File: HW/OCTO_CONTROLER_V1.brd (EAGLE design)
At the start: 65 x 56 mm, 58 parts, among them IC1 CXDM4060P, IC2 AOZ1284PI, J1 DC_POWER, Q1 CXDM4060P, Q10 DTDG23YP, Q2 CXDM4060P, Q3 DTC114EUA, Q4 DTC114EUA, Q5 DTC114EUA, Q6 DTC114EUA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

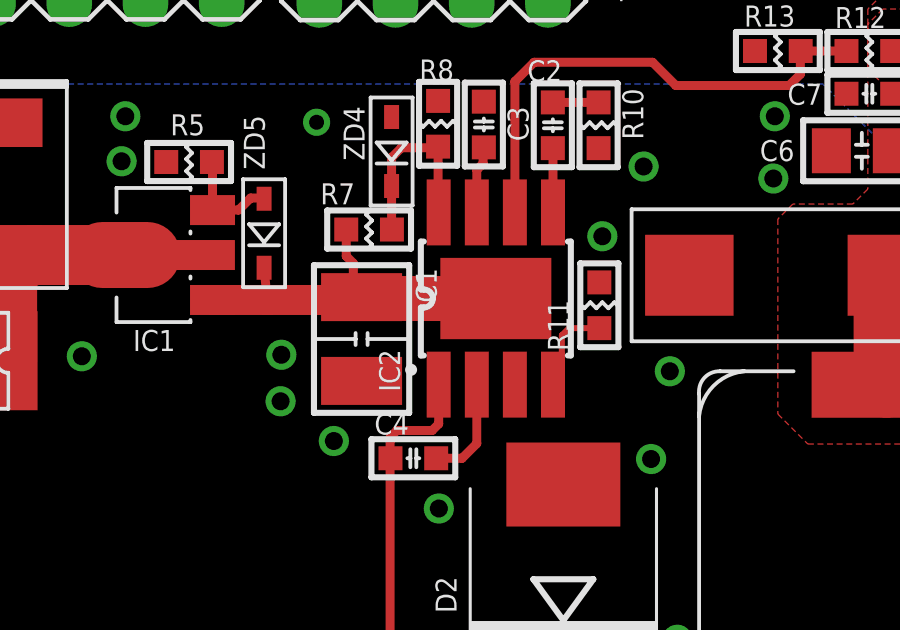
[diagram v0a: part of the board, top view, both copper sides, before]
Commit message: LED 저항값 수정
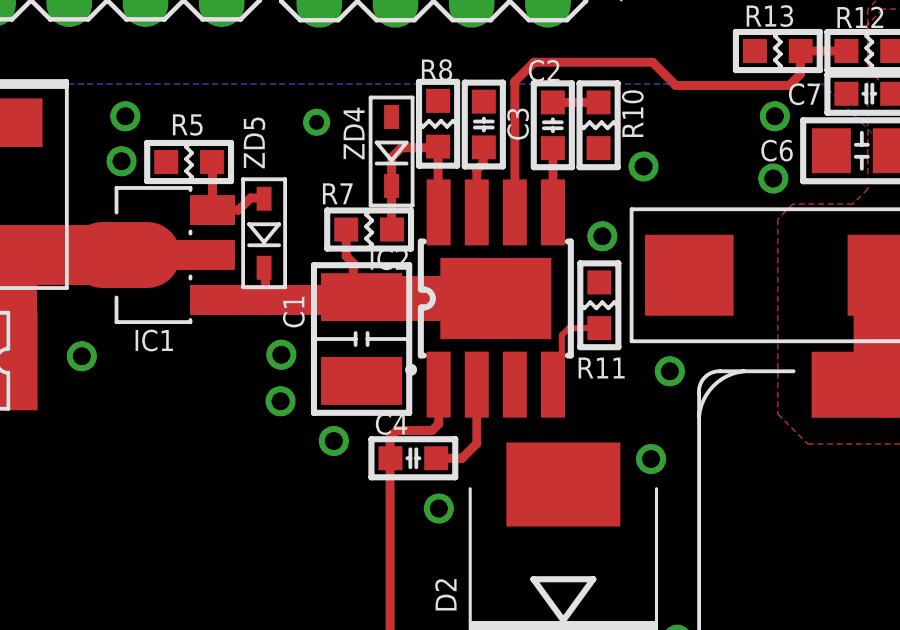
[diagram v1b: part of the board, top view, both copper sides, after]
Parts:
- R11: value 46.6k -> 47k
- R3, R4, R6, R9: value 220 -> 300
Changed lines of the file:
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@@
 </element>
 <element name="IC2" library="cona_lib" package="S08-EP1" value="AOZ1284PI" x="-14.9" y="23.35" smashed="yes">
-<attribute name="NAME" x="-18.092" y="20.245" size="0.7" layer="25" rot="R90"/>
+<attribute name="NAME" x="-17.745" y="25.008" size="0.7" layer="25" rot="R180"/>
 <attribute name="VALUE" x="-11.263" y="21.445" size="0.7" layer="27" rot="R90"/>
 </element>
@@
 <attribute name="VALUE" x="-11.476" y="27.601" size="0.7" layer="27" rot="R90"/>
 </element>
-<element name="R11" library="cona_lib" package="R0603" value="46.6k" x="-11.45" y="23.125" smashed="yes" rot="R90">
-<attribute name="NAME" x="-12.466" y="21.601" size="0.7" layer="25" rot="R90"/>
+<element name="R11" library="cona_lib" package="R0603" value="47k" x="-11.45" y="23.125" smashed="yes" rot="R90">
+<attribute name="NAME" x="-10.526" y="21.384" size="0.7" layer="25" rot="R180"/>
 <attribute name="VALUE" x="-9.926" y="21.601" size="0.7" layer="27" ratio="10" rot="R90"/>
 </element>
@@
 </element>
 <element name="C1" library="cona_lib" package="C3225" value="10uF/35V" x="-19.375" y="22" smashed="yes" rot="R270">
-<attribute name="NAME" x="-17.568" y="24.361" size="0.7" layer="25" rot="R270"/>
+<attribute name="NAME" x="-21.282" y="22.339" size="0.7" layer="25" rot="R90"/>
 <attribute name="VALUE" x="-21.915" y="24.286" size="0.6096" layer="27" ratio="10" rot="R270"/>
 </element>
@@
 <attribute name="VALUE" x="-30.865" y="5.95" size="0.7" layer="27" rot="R270"/>
 </element>
-<element name="R6" library="cona_lib" package="R0603" value="220" x="-32.975" y="-3.2" smashed="yes" rot="R90">
+<element name="R6" library="cona_lib" package="R0603" value="300" x="-32.975" y="-3.2" smashed="yes" rot="R90">
 <attribute name="NAME" x="-32.134" y="-2.776" size="0.7" layer="25" rot="R270"/>
 <attribute name="VALUE" x="-31.451" y="-4.724" size="0.7" layer="27" ratio="10" rot="R90"/>
 </element>
-<element name="R9" library="cona_lib" package="R0603" value="220" x="-34.55" y="-3.2" smashed="yes" rot="R90">
+<element name="R9" library="cona_lib" package="R0603" value="300" x="-34.55" y="-3.2" smashed="yes" rot="R90">
 <attribute name="NAME" x="-35.366" y="-3.924" size="0.7" layer="25" rot="R90"/>
 <attribute name="VALUE" x="-33.026" y="-4.724" size="0.7" layer="27" ratio="10" rot="R90"/>
@@
 <attribute name="VALUE" x="-33.72" y="2.7" size="0.8" layer="27" rot="R180"/>
 </element>
-<element name="R3" library="cona_lib" package="R0603" value="220" x="-7.375" y="-3.375" smashed="yes" rot="R90">
+<element name="R3" library="cona_lib" package="R0603" value="300" x="-7.375" y="-3.375" smashed="yes" rot="R90">
 <attribute name="NAME" x="-6.484" y="-3.226" size="0.7" layer="25" rot="R270"/>
 <attribute name="VALUE" x="-5.851" y="-4.899" size="0.7" layer="27" ratio="10" rot="R90"/>
 </element>
-<element name="R4" library="cona_lib" package="R0603" value="220" x="-8.9" y="-3.375" smashed="yes" rot="R90">
+<element name="R4" library="cona_lib" package="R0603" value="300" x="-8.9" y="-3.375" smashed="yes" rot="R90">
 <attribute name="NAME" x="-9.841" y="-4.374" size="0.7" layer="25" rot="R90"/>
 <attribute name="VALUE" x="-7.376" y="-4.899" size="0.7" layer="27" ratio="10" rot="R90"/>
